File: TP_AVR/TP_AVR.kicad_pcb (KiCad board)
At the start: 2 copper layers, 42.4 x 60.4 mm, 30 parts, among them J1 Conn_02x20_Counter_Clockwise, M1 ProMicro, U1 74HC238, U2 74HC238

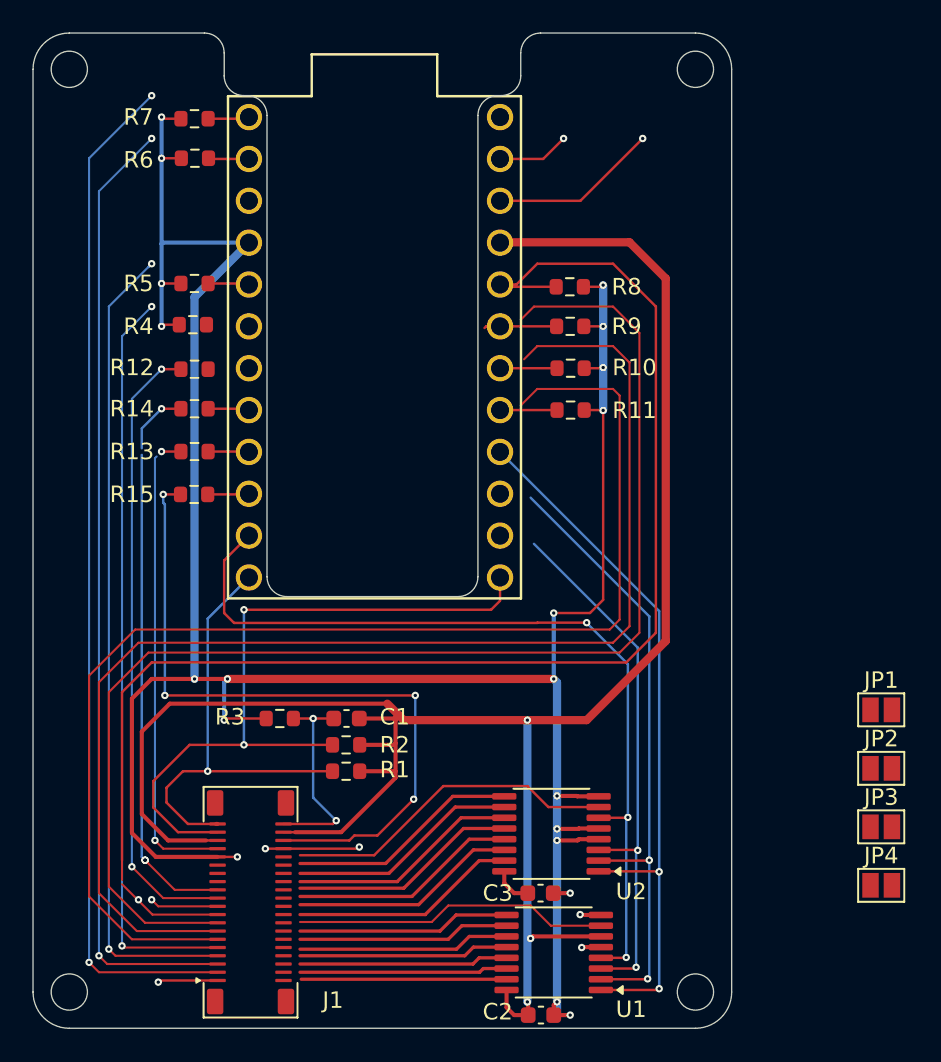
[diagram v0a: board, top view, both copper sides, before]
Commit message: Finished up board files
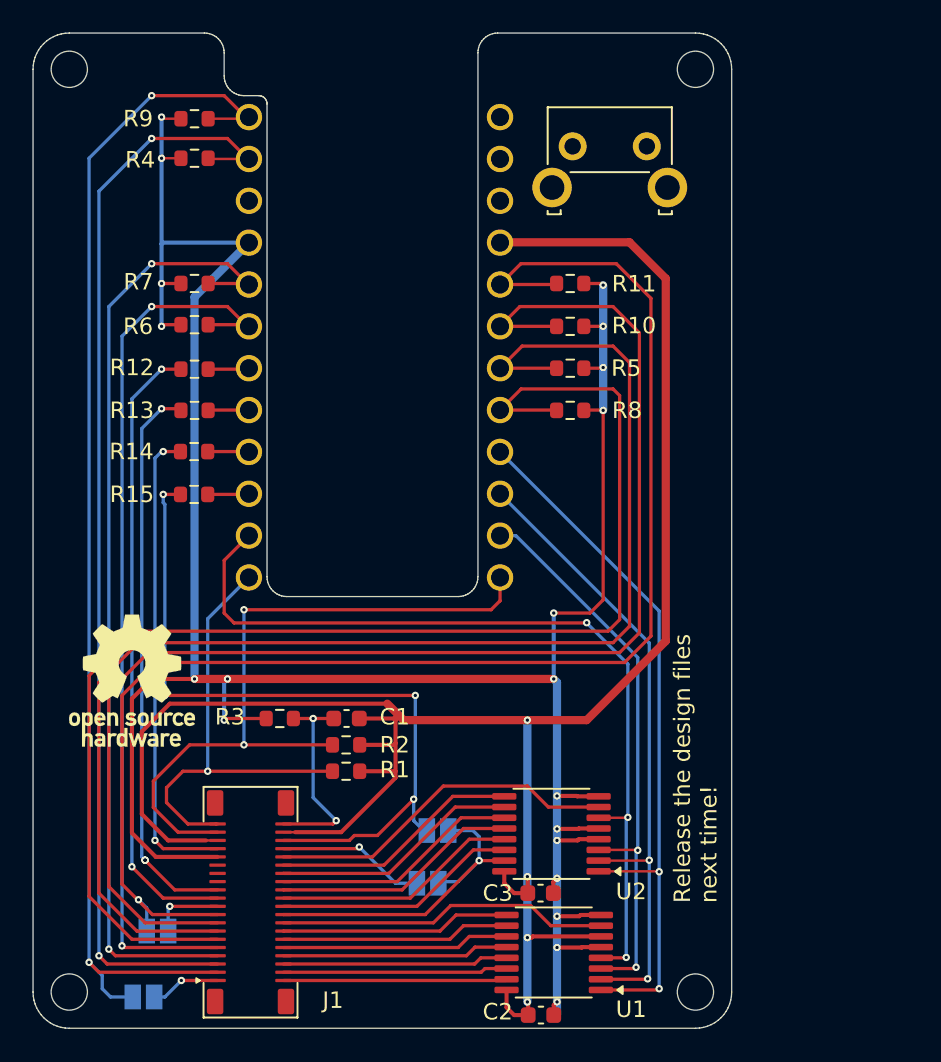
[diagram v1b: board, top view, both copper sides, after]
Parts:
- added REF**: OSHW-Logo_7.5x8mm_SilkScreen, Symbol:OSHW-Logo_7.5x8mm_SilkScreen, F.Cu at (84.8, 119.1)
- added SW1: SW_SPST, Button_Switch_THT:SW_SPST_Omron_B3F-315x_Angled, F.Cu at (111.5, 86.7)
- JP1, JP2, JP3, JP4: moved to B.Cu
- moved JP4 45.3 mm to (85.5, 138.3), turned to 180 degrees
- moved JP3 44.4 mm to (86.3, 134.3), turned to 180 degrees
- moved JP2 28.4 mm to (102.8, 131.4)
- moved JP1 27.9 mm to (103.3, 128.2)
- moved R9 26.0 mm to (88.6, 85.0), turned to 180 degrees
- moved R5 23.4 mm to (111.4, 100.1), turned to 0 degrees
- moved R4 10.1 mm to (88.6, 87.4)
- moved R6 10.1 mm to (88.6, 97.5)
- moved R7 10.0 mm to (88.6, 95.0)
- moved R11 7.68 mm to (111.4, 95.0)
- moved R8 7.50 mm to (111.4, 102.7)
- moved R14 2.60 mm to (88.6, 105.2)
- moved R10 2.54 mm to (111.4, 97.6)
- moved R13 2.50 mm to (88.6, 102.7)
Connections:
- J1 pad 1: unconnected-(J1-Pin_1-Pad1) -> JPR_CONF0
- J1 pad 10: COL3 -> COL4
- J1 pad 12: COL7 -> COL5
- J1 pad 14: COL2 -> COL6
- J1 pad 16: COL10 -> COL7
- J1 pad 18: COL1 -> COL8
- J1 pad 19: unconnected-(J1-Pin_19-Pad19) -> JPR_CONF1
- J1 pad 2: COL4 -> COL0
- J1 pad 22: COL0 -> COL10
- J1 pad 26: COL14 -> COL12
- J1 pad 28: COL12 -> COL13
- J1 pad 30: COL15 -> COL14
- J1 pad 32: COL13 -> COL15
- J1 pad 34: GND -> JPR_CONF2
- J1 pad 4: COL5 -> COL1
- J1 pad 6: COL8 -> COL2
- J1 pad 8: COL6 -> COL3
- JP1 pad 1: unconnected-(JP1-A-Pad1) -> LEDK3
- JP1 pad 2: unconnected-(JP1-B-Pad2) -> COL8
- JP2 pad 1: unconnected-(JP2-A-Pad1) -> JPR_CONF2
- JP2 pad 2: unconnected-(JP2-B-Pad2) -> COL8
- JP3 pad 1: unconnected-(JP3-A-Pad1) -> JPR_CONF1
- JP3 pad 2: unconnected-(JP3-B-Pad2) -> ROW7
- JP4 pad 1: unconnected-(JP4-A-Pad1) -> JPR_CONF0
- JP4 pad 2: unconnected-(JP4-B-Pad2) -> ROW5
- M1 pad 1: ROW3 -> ROW5
- M1 pad 14: S1 -> S2
- M1 pad 15: S2 -> S1
- M1 pad 17: ROW7 -> ROW4
- M1 pad 18: ROW6 -> ROW1
- M1 pad 19: ROW5 -> ROW6
- M1 pad 2: ROW2 -> ROW0
- M1 pad 20: ROW4 -> ROW7
- M1 pad 22: unconnected-(M1-RST-Pad22) -> Net-(M1-RST)
- M1 pad 5: ROW1 -> ROW3
- M1 pad 6: ROW0 -> ROW2
- M1 pad 8: LED_NUM -> LED_SCRL
- M1 pad 9: LED_SCRL -> LED_NUM
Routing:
- net ROW7: track 10.0 -> 88.0 mm
- net ROW4: track 155.7 -> 80.9 mm
- net unconnected-(M1-RST-Pad22): track 10.2 -> 0.00 mm, vias 1 -> 0
- net JPR_CONF2: track 0.00 -> 9.05 mm, vias 0 -> 1
- net ROW0: track 58.3 -> 67.2 mm
- net ROW5: track 66.6 -> 75.0 mm
- net GND: track 171.8 -> 163.5 mm, vias 25 -> 20
- net COL8: track 13.8 -> 21.3 mm, vias 0 -> 1
- net ROW2: track 47.9 -> 54.3 mm
- net ROW3: track 52.1 -> 58.5 mm
- net JPR_CONF1: track 0.00 -> 4.44 mm, vias 0 -> 1
- net JPR_CONF0: track 0.00 -> 4.26 mm, vias 0 -> 1
- net unconnected-(J1-Pin_19-Pad19): track 4.17 -> 0.00 mm, vias 1 -> 0
- net unconnected-(J1-Pin_1-Pad1): track 3.64 -> 0.00 mm, vias 1 -> 0
- net LEDK1: track 31.0 -> 34.3 mm
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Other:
- outline, holes or cut-outs redrawn
- board text added: "Release the design files next time!"

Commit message: bill of materials, board exported
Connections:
- SW1 pad 1: Net-(M1-RST) -> GND
- SW1 pad 2: GND -> Net-(M1-RST)
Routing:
- net Net-(M1-RST): track 0.00 -> 10.9 mm
- net GND: track 163.5 -> 167.5 mm
- net LEDK1: vias 3 -> 2
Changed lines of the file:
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@@
 			(layers "*.Cu" "*.Mask")
 			(remove_unused_layers no)
-			(net "Net-(M1-RST)")
+			(net "GND")
 			(pinfunction "A_1")
 			(pintype "passive")
@@
 			(layers "*.Cu" "*.Mask")
 			(remove_unused_layers no)
-			(net "GND")
+			(net "Net-(M1-RST)")
 			(pinfunction "B_2")
 			(pintype "passive")
@@
 	)
 	(segment
+		(start 111.943528 90.781471)
+		(end 116.049999 86.675)
+		(width 0.25)
+		(layer "F.Cu")
+		(net "Net-(M1-RST)")
+	)
+	(segment
+		(start 107.942427 90.781471)
+		(end 111.943528 90.781471)
+		(width 0.25)
+		(layer "F.Cu")
+		(net "Net-(M1-RST)")
+	)
+	(segment
+		(start 107.142428 89.981472)
+		(end 107.942427 90.781471)
+		(width 0.25)
+		(layer "F.Cu")
+		(net "Net-(M1-RST)")
+	)
+	(segment
 		(start 113.3 95.2)
 		(end 113.4 95.1)
@@
 	)
 	(segment
+		(start 107.142428 87.441472)
+		(end 110.783527 87.441472)
+		(width 0.25)
+		(layer "F.Cu")
+		(net "GND")
+	)
+	(segment
+		(start 110.783527 87.441472)
+		(end 111.549999 86.675)
+		(width 0.25)
+		(layer "F.Cu")
+		(net "GND")
+	)
+	(segment
 		(start 112.125 135.275)
 		(end 113.2625 135.275)
@@
 	)
 	(segment
-		(start 110.6 138.6)
-		(end 110.6 139.4)
-		(width 0.5)
-		(layer "B.Cu")
-		(net "GND")
-	)
-	(segment
 		(start 88.6 95.8239)
 		(end 88.6 119)
@@
 		(net "LEDK1")
 	)
-	(via
-		(at 85.6 130)
-		(size 0.45)
-		(drill 0.2)
-		(layers "F.Cu" "B.Cu")
-		(net "LEDK1")
-	)
